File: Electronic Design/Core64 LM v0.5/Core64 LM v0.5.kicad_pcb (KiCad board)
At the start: 2 copper layers, 85 x 85 mm, 67 parts, among them J1 Digi-Key 77311-420-36LF-ND, J2 Digi-Key 77311-420-36LF-ND

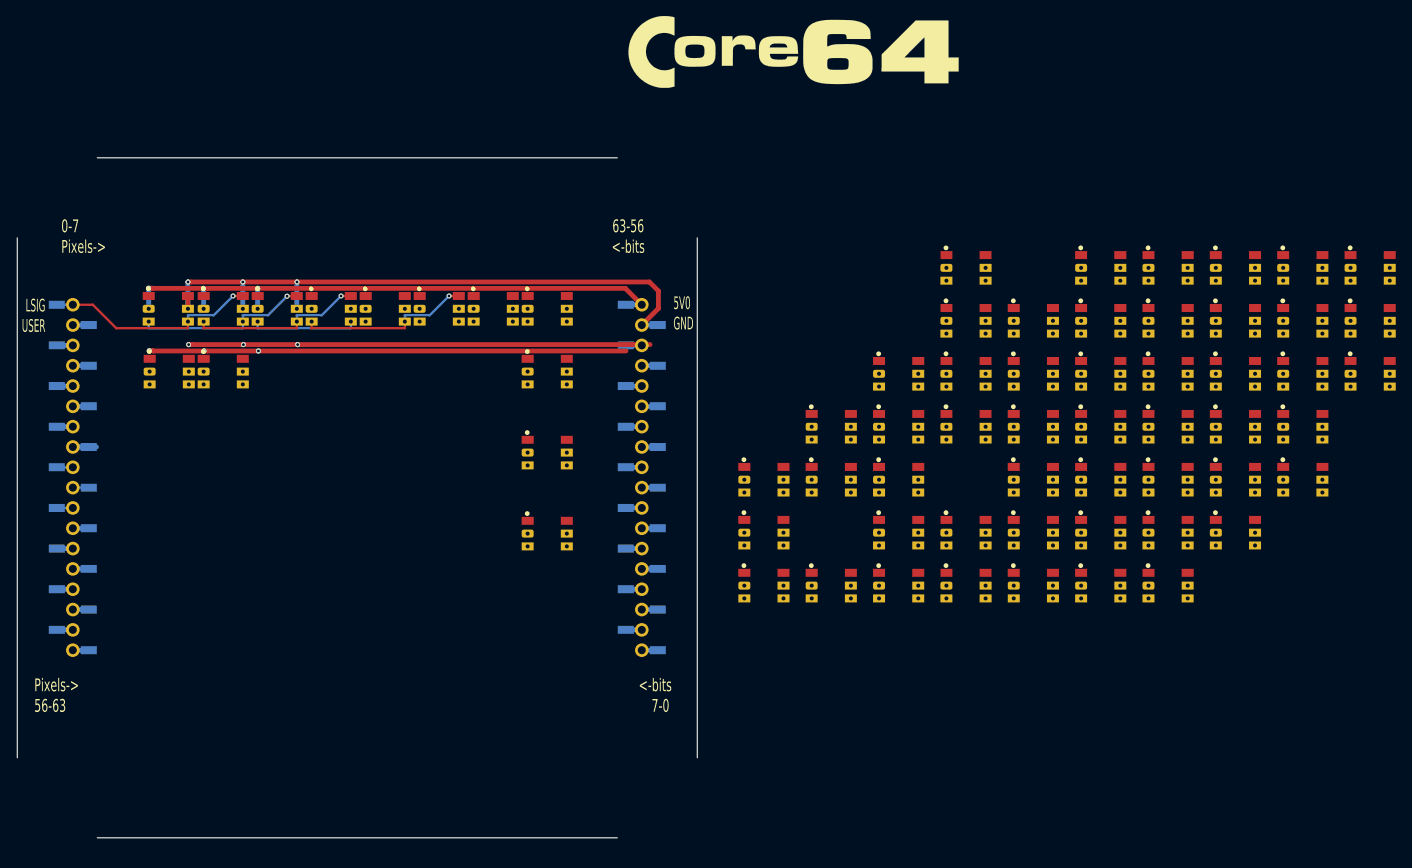
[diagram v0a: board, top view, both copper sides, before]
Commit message: Layout LED Matrix and add WS2812/13 data sheets
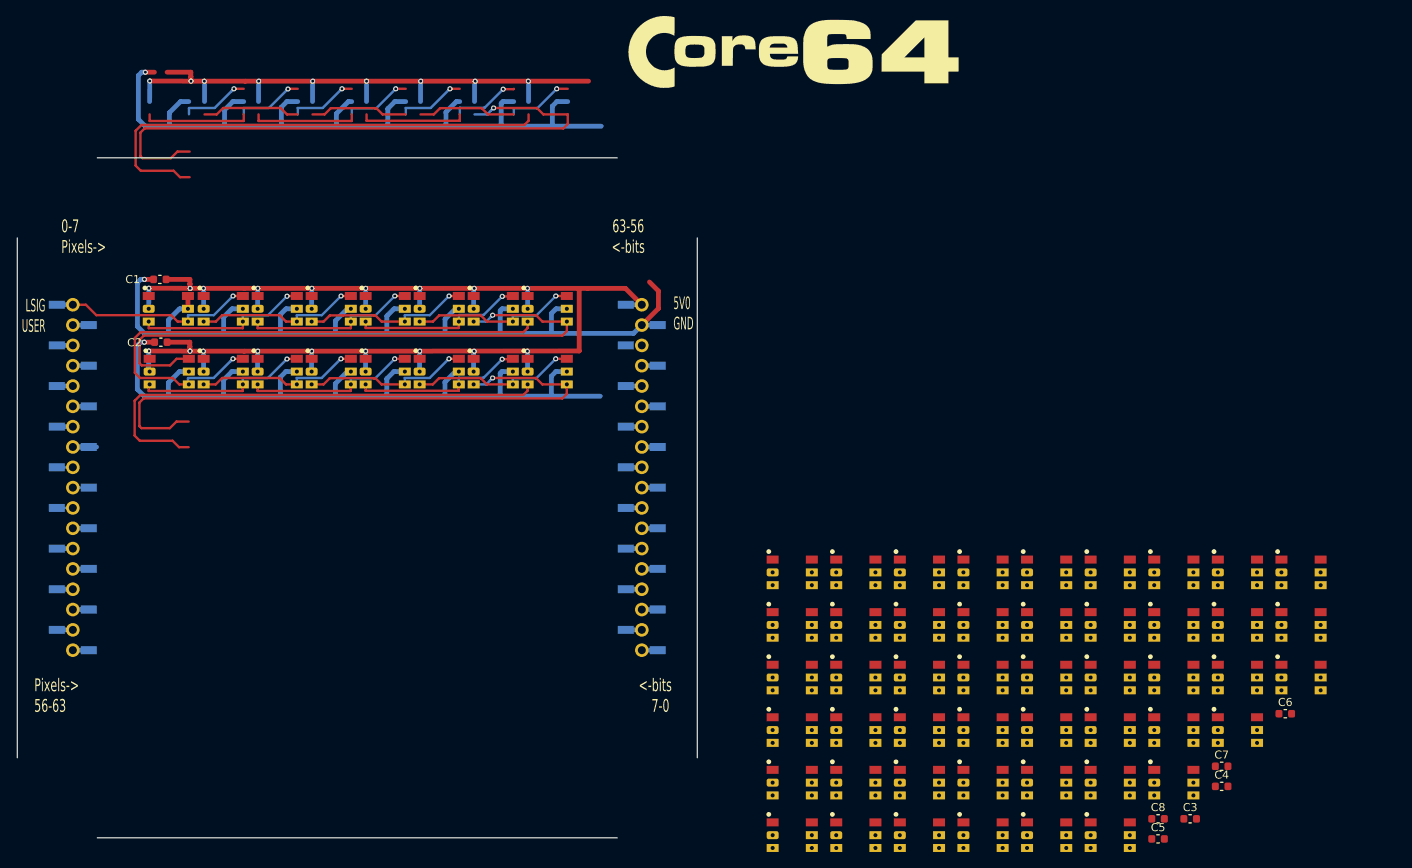
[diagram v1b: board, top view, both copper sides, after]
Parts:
- added C1: 0.1uF, Capacitor_SMD:C_0603_1608Metric, F.Cu at (-24.7, -27.3)
- added C2: 0.1uF, Capacitor_SMD:C_0603_1608Metric, F.Cu at (-24.6, -19.4)
- added C3: 0.1uF, Capacitor_SMD:C_0603_1608Metric, F.Cu at (104.1, 40.1)
- added C4: 0.1uF, Capacitor_SMD:C_0603_1608Metric, F.Cu at (108.0, 36.1)
- added C5: 0.1uF, Capacitor_SMD:C_0603_1608Metric, F.Cu at (100.1, 42.6)
- added C6: 0.1uF, Capacitor_SMD:C_0603_1608Metric, F.Cu at (116.0, 27.0)
- added C7: 0.1uF, Capacitor_SMD:C_0603_1608Metric, F.Cu at (108.0, 33.6)
- added C8: 0.1uF, Capacitor_SMD:C_0603_1608Metric, F.Cu at (100.1, 40.1)
- moved D11 87.1 mm to (-10.0, -15.8)
- moved D61 81.6 mm to (54.4, 22.5)
- moved D44 81.4 mm to (78.2, 42.2)
- moved D51 72.1 mm to (94.1, 35.6)
- moved D64 65.4 mm to (70.3, 42.2)
- moved D21 65.1 mm to (54.4, 35.6)
- moved D56 62.7 mm to (102.1, 35.6)
- moved D55 62.5 mm to (94.1, 42.2)
- moved D60 61.1 mm to (62.3, 15.9)
- moved D15 59.4 mm to (17.0, -15.8)
- moved D24 58.6 mm to (78.2, 15.9)
- moved D14 57.4 mm to (10.2, -15.8)
- moved D63 56.6 mm to (54.4, 15.9)
- moved D13 56.2 mm to (3.49, -15.8)
- moved D23 56.0 mm to (70.3, 22.5)
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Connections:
- D10 pad 2: Net-(D10-Pad2) -> 5V0
- D10 pad 5: Net-(D10-Pad5) -> GND
- D10 pad 6: Net-(D10-Pad6) -> R1DO
- D11 pad 2: Net-(D11-Pad2) -> 5V0
- D11 pad 4: Net-(D11-Pad4) -> Net-(D10-Pad3)
- D11 pad 5: Net-(D11-Pad5) -> GND
- D11 pad 6: Net-(D11-Pad6) -> Net-(D10-Pad4)
- D12 pad 2: Net-(D12-Pad2) -> 5V0
- D12 pad 4: Net-(D12-Pad4) -> Net-(D11-Pad3)
- D12 pad 5: Net-(D12-Pad5) -> GND
- D12 pad 6: Net-(D12-Pad6) -> Net-(D10-Pad3)
- D13 pad 2: Net-(D13-Pad2) -> 5V0
- D13 pad 4: Net-(D13-Pad4) -> Net-(D12-Pad3)
- D13 pad 5: Net-(D13-Pad5) -> GND
- D13 pad 6: Net-(D13-Pad6) -> Net-(D11-Pad3)
- D14 pad 2: Net-(D14-Pad2) -> 5V0
- D14 pad 4: Net-(D14-Pad4) -> Net-(D13-Pad3)
- D14 pad 5: Net-(D14-Pad5) -> GND
- D14 pad 6: Net-(D14-Pad6) -> Net-(D12-Pad3)
- D15 pad 2: Net-(D15-Pad2) -> 5V0
- D15 pad 3: Net-(D15-Pad3) -> R2DIN
- D15 pad 4: Net-(D15-Pad4) -> Net-(D14-Pad3)
- D15 pad 5: Net-(D15-Pad5) -> GND
- D15 pad 6: Net-(D15-Pad6) -> Net-(D13-Pad3)
- D16 pad 2: Net-(D16-Pad2) -> 5V0
- D16 pad 3: Net-(D16-Pad3) -> R2DO
- D16 pad 4: Net-(D16-Pad4) -> R2DIN
- D16 pad 5: Net-(D16-Pad5) -> GND
- D16 pad 6: Net-(D16-Pad6) -> Net-(D14-Pad3)
- D17 pad 2: Net-(D17-Pad2) -> 5V0
- D17 pad 4: Net-(D17-Pad4) -> R2DO
- D17 pad 5: Net-(D17-Pad5) -> GND
- D17 pad 6: Net-(D17-Pad6) -> R2DIN
- D18 pad 2: Net-(D18-Pad2) -> 5V0
- D18 pad 4: Net-(D18-Pad4) -> Net-(D17-Pad3)
- D18 pad 5: Net-(D18-Pad5) -> GND
- D18 pad 6: Net-(D18-Pad6) -> R2DO
- D19 pad 2: Net-(D19-Pad2) -> 5V0
- D19 pad 4: Net-(D19-Pad4) -> Net-(D18-Pad3)
- D19 pad 5: Net-(D19-Pad5) -> GND
- D19 pad 6: Net-(D19-Pad6) -> Net-(D17-Pad3)
- D20 pad 2: Net-(D20-Pad2) -> 5V0
- D20 pad 4: Net-(D20-Pad4) -> Net-(D19-Pad3)
- D20 pad 5: Net-(D20-Pad5) -> GND
- D20 pad 6: Net-(D20-Pad6) -> Net-(D18-Pad3)
- D21 pad 2: Net-(D21-Pad2) -> 5V0
- D21 pad 4: Net-(D21-Pad4) -> Net-(D20-Pad3)
- D21 pad 5: Net-(D21-Pad5) -> GND
- D21 pad 6: Net-(D21-Pad6) -> Net-(D19-Pad3)
- D22 pad 2: Net-(D22-Pad2) -> 5V0
- D22 pad 4: Net-(D22-Pad4) -> Net-(D21-Pad3)
- D22 pad 5: Net-(D22-Pad5) -> GND
- D22 pad 6: Net-(D22-Pad6) -> Net-(D20-Pad3)
- D23 pad 2: Net-(D23-Pad2) -> 5V0
- D23 pad 3: Net-(D23-Pad3) -> R3DIN
- D23 pad 4: Net-(D23-Pad4) -> Net-(D22-Pad3)
- D23 pad 5: Net-(D23-Pad5) -> GND
- D23 pad 6: Net-(D23-Pad6) -> Net-(D21-Pad3)
- D24 pad 2: Net-(D24-Pad2) -> 5V0
- D24 pad 3: Net-(D24-Pad3) -> R3DO
- D24 pad 4: Net-(D24-Pad4) -> R3DIN
- D24 pad 5: Net-(D24-Pad5) -> GND
- D24 pad 6: Net-(D24-Pad6) -> Net-(D22-Pad3)
- D25 pad 2: Net-(D25-Pad2) -> 5V0
- D25 pad 4: Net-(D25-Pad4) -> R3DO
- D25 pad 5: Net-(D25-Pad5) -> GND
- D25 pad 6: Net-(D25-Pad6) -> R3DIN
- D26 pad 2: Net-(D26-Pad2) -> 5V0
- D26 pad 4: Net-(D26-Pad4) -> Net-(D25-Pad3)
- D26 pad 5: Net-(D26-Pad5) -> GND
- D26 pad 6: Net-(D26-Pad6) -> R3DO
- D27 pad 2: Net-(D27-Pad2) -> 5V0
- D27 pad 4: Net-(D27-Pad4) -> Net-(D26-Pad3)
- D27 pad 5: Net-(D27-Pad5) -> GND
- D27 pad 6: Net-(D27-Pad6) -> Net-(D25-Pad3)
- D28 pad 2: Net-(D28-Pad2) -> 5V0
- D28 pad 4: Net-(D28-Pad4) -> Net-(D27-Pad3)
- D28 pad 5: Net-(D28-Pad5) -> GND
- D28 pad 6: Net-(D28-Pad6) -> Net-(D26-Pad3)
- D29 pad 2: Net-(D29-Pad2) -> 5V0
- D29 pad 4: Net-(D29-Pad4) -> Net-(D28-Pad3)
- D29 pad 5: Net-(D29-Pad5) -> GND
- D29 pad 6: Net-(D29-Pad6) -> Net-(D27-Pad3)
- D30 pad 2: Net-(D30-Pad2) -> 5V0
- D30 pad 4: Net-(D30-Pad4) -> Net-(D29-Pad3)
- D30 pad 5: Net-(D30-Pad5) -> GND
- D30 pad 6: Net-(D30-Pad6) -> Net-(D28-Pad3)
- D31 pad 2: Net-(D31-Pad2) -> 5V0
- D31 pad 3: Net-(D31-Pad3) -> R4DIN
- D31 pad 4: Net-(D31-Pad4) -> Net-(D30-Pad3)
- D31 pad 5: Net-(D31-Pad5) -> GND
- D31 pad 6: Net-(D31-Pad6) -> Net-(D29-Pad3)
- D32 pad 2: Net-(D32-Pad2) -> 5V0
- D32 pad 3: Net-(D32-Pad3) -> R4DO
- D32 pad 4: Net-(D32-Pad4) -> R4DIN
- D32 pad 5: Net-(D32-Pad5) -> GND
- D32 pad 6: Net-(D32-Pad6) -> Net-(D30-Pad3)
- D33 pad 2: Net-(D33-Pad2) -> 5V0
- D33 pad 4: Net-(D33-Pad4) -> R4DO
- D33 pad 5: Net-(D33-Pad5) -> GND
- D33 pad 6: Net-(D33-Pad6) -> R4DIN
- D34 pad 2: Net-(D34-Pad2) -> 5V0
- D34 pad 4: Net-(D34-Pad4) -> Net-(D33-Pad3)
- D34 pad 5: Net-(D34-Pad5) -> GND
- D34 pad 6: Net-(D34-Pad6) -> R4DO
- D35 pad 2: Net-(D35-Pad2) -> 5V0
- D35 pad 4: Net-(D35-Pad4) -> Net-(D34-Pad3)
- D35 pad 5: Net-(D35-Pad5) -> GND
- D35 pad 6: Net-(D35-Pad6) -> Net-(D33-Pad3)
- D36 pad 2: Net-(D36-Pad2) -> 5V0
- D36 pad 4: Net-(D36-Pad4) -> Net-(D35-Pad3)
- D36 pad 5: Net-(D36-Pad5) -> GND
- D36 pad 6: Net-(D36-Pad6) -> Net-(D34-Pad3)
- D37 pad 2: Net-(D37-Pad2) -> 5V0
- D37 pad 4: Net-(D37-Pad4) -> Net-(D36-Pad3)
- D37 pad 5: Net-(D37-Pad5) -> GND
- D37 pad 6: Net-(D37-Pad6) -> Net-(D35-Pad3)
- D38 pad 2: Net-(D38-Pad2) -> 5V0
- D38 pad 4: Net-(D38-Pad4) -> Net-(D37-Pad3)
- D38 pad 5: Net-(D38-Pad5) -> GND
- D38 pad 6: Net-(D38-Pad6) -> Net-(D36-Pad3)
- D39 pad 2: Net-(D39-Pad2) -> 5V0
- D39 pad 3: Net-(D39-Pad3) -> R5DIN
- D39 pad 4: Net-(D39-Pad4) -> Net-(D38-Pad3)
- D39 pad 5: Net-(D39-Pad5) -> GND
- D39 pad 6: Net-(D39-Pad6) -> Net-(D37-Pad3)
- D40 pad 2: Net-(D40-Pad2) -> 5V0
- D40 pad 3: Net-(D40-Pad3) -> R5DO
- D40 pad 4: Net-(D40-Pad4) -> R5DIN
- D40 pad 5: Net-(D40-Pad5) -> GND
- D40 pad 6: Net-(D40-Pad6) -> Net-(D38-Pad3)
- D41 pad 2: Net-(D41-Pad2) -> 5V0
- D41 pad 4: Net-(D41-Pad4) -> R5DO
- D41 pad 5: Net-(D41-Pad5) -> GND
- D41 pad 6: Net-(D41-Pad6) -> R5DIN
- D42 pad 2: Net-(D42-Pad2) -> 5V0
- D42 pad 4: Net-(D42-Pad4) -> Net-(D41-Pad3)
- D42 pad 5: Net-(D42-Pad5) -> GND
- D42 pad 6: Net-(D42-Pad6) -> R5DO
- D43 pad 2: Net-(D43-Pad2) -> 5V0
- D43 pad 4: Net-(D43-Pad4) -> Net-(D42-Pad3)
- D43 pad 5: Net-(D43-Pad5) -> GND
- D43 pad 6: Net-(D43-Pad6) -> Net-(D41-Pad3)
- D44 pad 2: Net-(D44-Pad2) -> 5V0
- D44 pad 4: Net-(D44-Pad4) -> Net-(D43-Pad3)
- D44 pad 5: Net-(D44-Pad5) -> GND
- D44 pad 6: Net-(D44-Pad6) -> Net-(D42-Pad3)
- D45 pad 2: Net-(D45-Pad2) -> 5V0
- D45 pad 4: Net-(D45-Pad4) -> Net-(D44-Pad3)
- D45 pad 5: Net-(D45-Pad5) -> GND
- D45 pad 6: Net-(D45-Pad6) -> Net-(D43-Pad3)
- D46 pad 2: Net-(D46-Pad2) -> 5V0
- D46 pad 4: Net-(D46-Pad4) -> Net-(D45-Pad3)
- D46 pad 5: Net-(D46-Pad5) -> GND
- D46 pad 6: Net-(D46-Pad6) -> Net-(D44-Pad3)
- D47 pad 2: Net-(D47-Pad2) -> 5V0
- D47 pad 3: Net-(D47-Pad3) -> R6DIN
- D47 pad 4: Net-(D47-Pad4) -> Net-(D46-Pad3)
- D47 pad 5: Net-(D47-Pad5) -> GND
- D47 pad 6: Net-(D47-Pad6) -> Net-(D45-Pad3)
- D48 pad 2: Net-(D48-Pad2) -> 5V0
- D48 pad 3: Net-(D48-Pad3) -> R6DO
- D48 pad 4: Net-(D48-Pad4) -> R6DIN
- D48 pad 5: Net-(D48-Pad5) -> GND
- D48 pad 6: Net-(D48-Pad6) -> Net-(D46-Pad3)
- D49 pad 2: Net-(D49-Pad2) -> 5V0
- D49 pad 4: Net-(D49-Pad4) -> R6DO
- D49 pad 5: Net-(D49-Pad5) -> GND
- D49 pad 6: Net-(D49-Pad6) -> R6DIN
- D5 pad 2: Net-(D5-Pad2) -> 5V0
- D5 pad 4: Net-(D5-Pad4) -> Net-(D4-Pad3)
- D5 pad 5: Net-(D5-Pad5) -> GND
- D5 pad 6: Net-(D5-Pad6) -> Net-(D3-Pad3)
- D50 pad 2: Net-(D50-Pad2) -> 5V0
- D50 pad 4: Net-(D50-Pad4) -> Net-(D49-Pad3)
- D50 pad 5: Net-(D50-Pad5) -> GND
- D50 pad 6: Net-(D50-Pad6) -> R6DO
- D51 pad 2: Net-(D51-Pad2) -> 5V0
- D51 pad 4: Net-(D51-Pad4) -> Net-(D50-Pad3)
- D51 pad 5: Net-(D51-Pad5) -> GND
- D51 pad 6: Net-(D51-Pad6) -> Net-(D49-Pad3)
- D52 pad 2: Net-(D52-Pad2) -> 5V0
- D52 pad 4: Net-(D52-Pad4) -> Net-(D51-Pad3)
- D52 pad 5: Net-(D52-Pad5) -> GND
- D52 pad 6: Net-(D52-Pad6) -> Net-(D50-Pad3)
- D53 pad 2: Net-(D53-Pad2) -> 5V0
- D53 pad 4: Net-(D53-Pad4) -> Net-(D52-Pad3)
- D53 pad 5: Net-(D53-Pad5) -> GND
- D53 pad 6: Net-(D53-Pad6) -> Net-(D51-Pad3)
- D54 pad 2: Net-(D54-Pad2) -> 5V0
- D54 pad 4: Net-(D54-Pad4) -> Net-(D53-Pad3)
- D54 pad 5: Net-(D54-Pad5) -> GND
- D54 pad 6: Net-(D54-Pad6) -> Net-(D52-Pad3)
- D55 pad 2: Net-(D55-Pad2) -> 5V0
- D55 pad 3: Net-(D55-Pad3) -> R7DIN
- D55 pad 4: Net-(D55-Pad4) -> Net-(D54-Pad3)
- D55 pad 5: Net-(D55-Pad5) -> GND
- D55 pad 6: Net-(D55-Pad6) -> Net-(D53-Pad3)
- D56 pad 2: Net-(D56-Pad2) -> 5V0
- D56 pad 3: Net-(D56-Pad3) -> R7DO
- D56 pad 4: Net-(D56-Pad4) -> R7DIN
- D56 pad 5: Net-(D56-Pad5) -> GND
- D56 pad 6: Net-(D56-Pad6) -> Net-(D54-Pad3)
- D57 pad 2: Net-(D57-Pad2) -> 5V0
- D57 pad 4: Net-(D57-Pad4) -> R7DO
- D57 pad 5: Net-(D57-Pad5) -> GND
- D57 pad 6: Net-(D57-Pad6) -> R7DIN
- D58 pad 2: Net-(D58-Pad2) -> 5V0
- D58 pad 4: Net-(D58-Pad4) -> Net-(D57-Pad3)
- D58 pad 5: Net-(D58-Pad5) -> GND
- D58 pad 6: Net-(D58-Pad6) -> R7DO
- D59 pad 2: Net-(D59-Pad2) -> 5V0
- D59 pad 4: Net-(D59-Pad4) -> Net-(D58-Pad3)
- D59 pad 5: Net-(D59-Pad5) -> GND
- D59 pad 6: Net-(D59-Pad6) -> Net-(D57-Pad3)
- D6 pad 2: Net-(D6-Pad2) -> 5V0
- D6 pad 4: Net-(D6-Pad4) -> Net-(D5-Pad3)
- D6 pad 5: Net-(D6-Pad5) -> GND
- D6 pad 6: Net-(D6-Pad6) -> Net-(D4-Pad3)
- D60 pad 2: Net-(D60-Pad2) -> 5V0
- D60 pad 4: Net-(D60-Pad4) -> Net-(D59-Pad3)
- D60 pad 5: Net-(D60-Pad5) -> GND
- D60 pad 6: Net-(D60-Pad6) -> Net-(D58-Pad3)
- D61 pad 2: Net-(D61-Pad2) -> 5V0
- D61 pad 4: Net-(D61-Pad4) -> Net-(D60-Pad3)
- D61 pad 5: Net-(D61-Pad5) -> GND
- D61 pad 6: Net-(D61-Pad6) -> Net-(D59-Pad3)
- D62 pad 2: Net-(D62-Pad2) -> 5V0
- D62 pad 4: Net-(D62-Pad4) -> Net-(D61-Pad3)
- D62 pad 5: Net-(D62-Pad5) -> GND
- D62 pad 6: Net-(D62-Pad6) -> Net-(D60-Pad3)
- D63 pad 2: Net-(D63-Pad2) -> 5V0
- D63 pad 4: Net-(D63-Pad4) -> Net-(D62-Pad3)
- D63 pad 5: Net-(D63-Pad5) -> GND
- D63 pad 6: Net-(D63-Pad6) -> Net-(D61-Pad3)
- D64 pad 2: Net-(D64-Pad2) -> 5V0
- D64 pad 4: Net-(D64-Pad4) -> Net-(D63-Pad3)
- D64 pad 5: Net-(D64-Pad5) -> GND
- D64 pad 6: Net-(D64-Pad6) -> Net-(D62-Pad3)
- D7 pad 2: Net-(D7-Pad2) -> 5V0
- D7 pad 3: Net-(D7-Pad3) -> R1DIN
- D7 pad 4: Net-(D7-Pad4) -> Net-(D6-Pad3)
- D7 pad 5: Net-(D7-Pad5) -> GND
- D7 pad 6: Net-(D7-Pad6) -> Net-(D5-Pad3)
- D8 pad 2: Net-(D8-Pad2) -> 5V0
- D8 pad 3: Net-(D8-Pad3) -> R1DO
- D8 pad 4: Net-(D8-Pad4) -> R1DIN
- D8 pad 5: Net-(D8-Pad5) -> GND
- D8 pad 6: Net-(D8-Pad6) -> Net-(D6-Pad3)
- D9 pad 2: Net-(D9-Pad2) -> 5V0
- D9 pad 3: Net-(D9-Pad3) -> Net-(D10-Pad4)
- D9 pad 4: Net-(D9-Pad4) -> R1DO
- D9 pad 5: Net-(D9-Pad5) -> GND
- D9 pad 6: Net-(D9-Pad6) -> R1DIN
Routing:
- net (no net): track 81.5 -> 457.4 mm, vias 4 -> 18
- net GND: track 78.1 -> 220.5 mm, vias 3 -> 2
- net 5V0: track 72.2 -> 175.3 mm, vias 3 -> 18
- net R2DIN: track 0.00 -> 76.9 mm, vias 0 -> 1
- net R1DIN: track 0.00 -> 76.9 mm, vias 0 -> 1
- net R1DO: track 0.00 -> 70.7 mm, vias 0 -> 1
- net R2DO: track 0.00 -> 62.1 mm
- net Net-(J2-Pad3): track 59.4 -> 0.00 mm, vias 3 -> 0
- net Net-(D10-Pad4): track 0.00 -> 22.0 mm, vias 0 -> 1
- net Net-(D11-Pad3): track 0.00 -> 21.8 mm, vias 0 -> 1
- net Net-(D5-Pad3): track 0.00 -> 21.8 mm, vias 0 -> 1
- net Net-(D13-Pad3): track 0.00 -> 21.8 mm, vias 0 -> 1
- net Net-(D10-Pad3): track 0.00 -> 20.9 mm, vias 0 -> 1
- net Net-(D4-Pad3): track 0.00 -> 20.8 mm, vias 0 -> 1
- net Net-(D12-Pad3): track 0.00 -> 20.8 mm, vias 0 -> 1
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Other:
- board text added: "Center is 0,0 LED spacing is 6.75mm center-to-center, X and Y directions. LED just right and low of center is 3.375, 3.375 LED in upper left is -23.625, -23.625"

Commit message: Completed LED Matrix layout
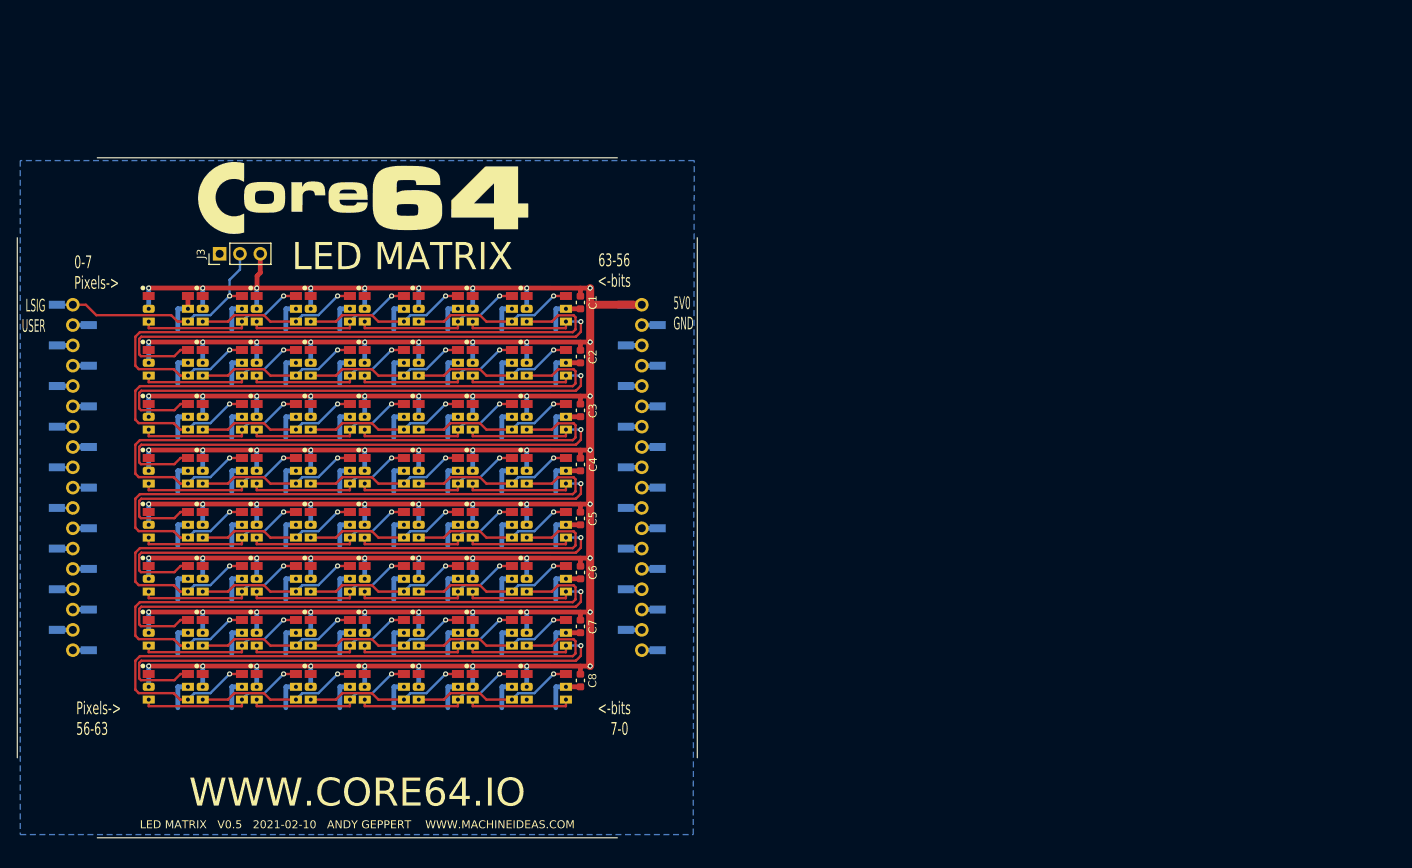
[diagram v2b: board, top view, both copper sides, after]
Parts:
- added J3: Conn_01x03_Male, Connector_PinHeader_2.54mm:PinHeader_1x03_P2.54mm_Vertical, F.Cu at (-17.2, -30.5)
- moved D49 141.8 mm to (-23.6, 16.9)
- moved D58 134.8 mm to (-16.9, 23.6)
- moved D57 133.7 mm to (-23.6, 23.6)
- moved D43 120.1 mm to (-10.1, 10.1)
- moved D42 119.1 mm to (-16.9, 10.1)
- moved D41 118.4 mm to (-23.6, 10.1)
- moved D25 110.5 mm to (-23.6, -3.38)
- moved D54 107.8 mm to (10.1, 16.9)
- moved D53 106.8 mm to (3.38, 16.9)
- moved D52 106.1 mm to (-3.38, 16.9)
- moved D50 106.1 mm to (-16.9, 16.9)
- moved D51 105.9 mm to (-10.1, 16.9)
- moved D33 99.3 mm to (-23.6, 3.38)
- moved D37 98.9 mm to (3.38, 3.38)
- moved D34 98.5 mm to (-16.9, 3.38)
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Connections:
- net USER renamed Net-(J1-Pad2)
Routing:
- net 5V0: track 175.3 -> 675.5 mm, vias 18 -> 72
- net (no net): track 457.4 -> 0.00 mm, vias 18 -> 0
- net R4DO: track 0.00 -> 82.3 mm, vias 0 -> 1
- net R7DO: track 0.00 -> 82.3 mm, vias 0 -> 1
- net R6DO: track 0.00 -> 82.3 mm, vias 0 -> 1
- net R5DO: track 0.00 -> 82.3 mm, vias 0 -> 1
- net R3DO: track 0.00 -> 82.3 mm, vias 0 -> 1
- net R5DIN: track 0.00 -> 80.6 mm, vias 0 -> 1
- net R6DIN: track 0.00 -> 80.6 mm, vias 0 -> 1
- net R3DIN: track 0.00 -> 80.6 mm, vias 0 -> 1
- net R7DIN: track 0.00 -> 80.6 mm, vias 0 -> 1
- net R4DIN: track 0.00 -> 80.6 mm, vias 0 -> 1
- net GND: track 220.5 -> 265.7 mm, vias 2 -> 0
- net Net-(D45-Pad3): track 0.00 -> 21.5 mm, vias 0 -> 1
- net Net-(D61-Pad3): track 0.00 -> 21.5 mm, vias 0 -> 1
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- added copper zone on B.Cu, net GND
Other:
- board text added: "LED MATRIX"
- board text added: "LED MATRIX V0.5 2021-02-10 ANDY GEPPERT WWW.MACHINEIDEAS.COM"
- board text added: "WWW.CORE64.IO"
- board text removed: "Core64.MachineIdeas.com"
- board text removed: "Interactive Core Memory"
- board text removed: "LED MATRIX V0.5 2021-02-10 ANDY GEPPERT"

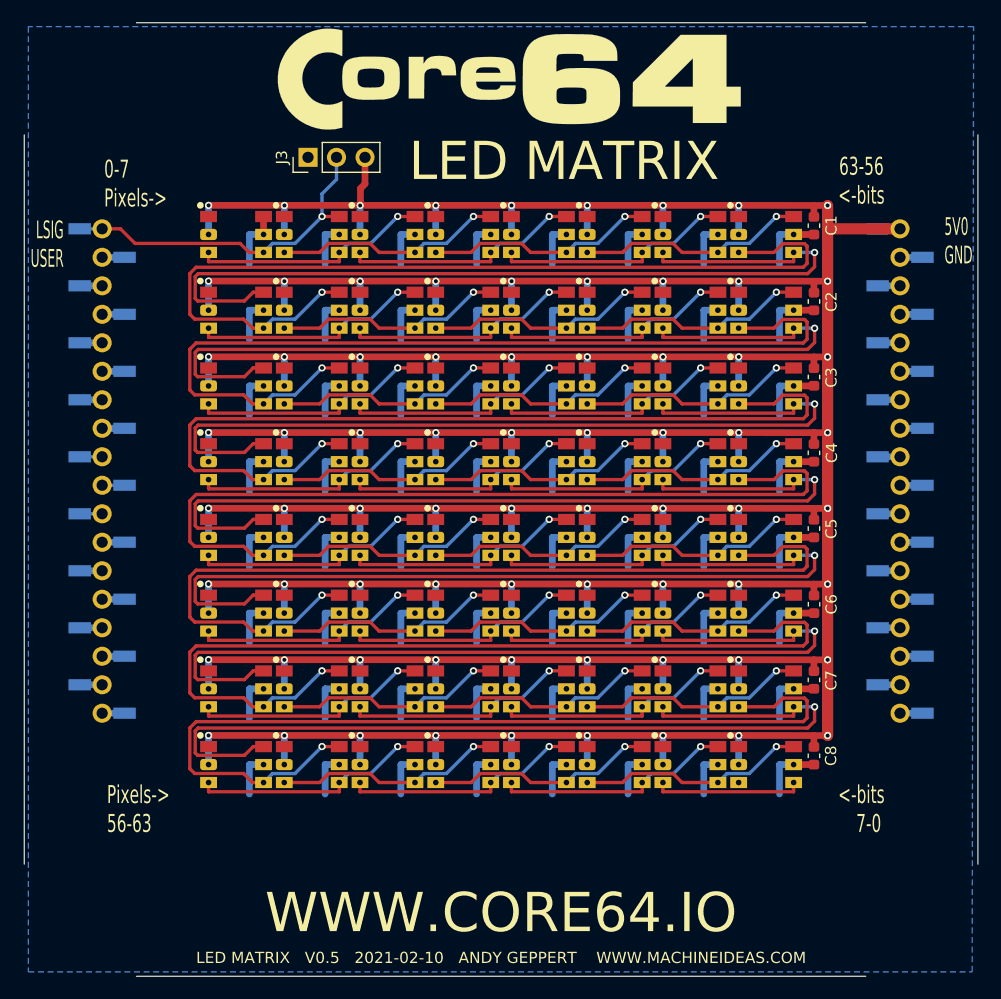
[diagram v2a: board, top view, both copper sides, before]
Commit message: Update core grid to 6.75mm square
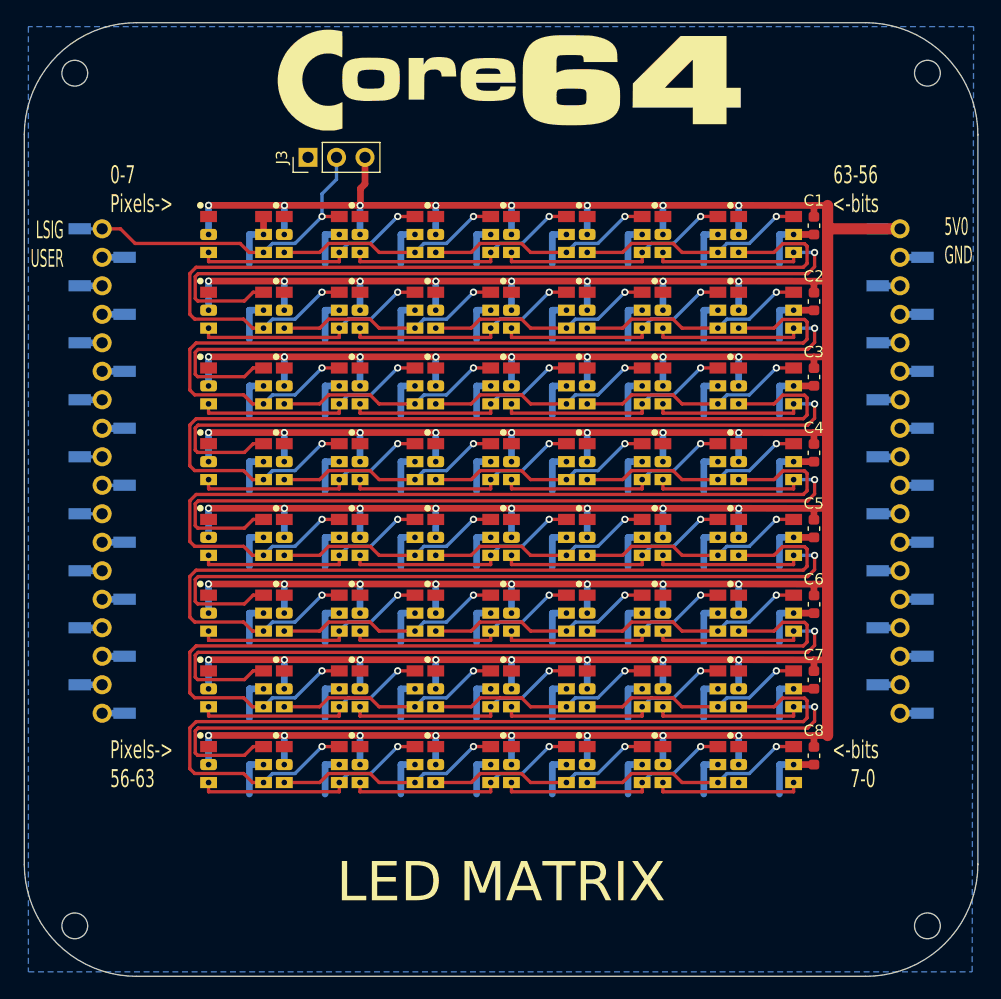
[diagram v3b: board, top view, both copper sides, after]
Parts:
- moved L1 0.10 mm to (2.62, -37.4)
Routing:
- net 5V0: vias 72 -> 64
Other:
- outline, holes or cut-outs redrawn
- board text added: "www.Core64.io"
- board text removed: "WWW.CORE64.IO"
